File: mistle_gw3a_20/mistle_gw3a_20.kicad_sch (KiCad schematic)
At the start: 55 parts, among them J1 SWD, J2 USB_C_Receptacle_USB2.0, SW1 Boot, U1 SY8113BADC, U2 W25Q64JVS, U3 USBLC6-2SC6, U4 RP2040, Y1 12MHz

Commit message: Update gw3a dev board
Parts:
- removed JP1: SRC D+, Jumper:SolderJumper-3_P1.3mm_Bridged12_RoundedPad1.0x1.5mm, symbol Jumper:SolderJumper_3_Bridged12
- removed JP2: SRC D-, Jumper:SolderJumper-3_P1.3mm_Bridged12_RoundedPad1.0x1.5mm, symbol Jumper:SolderJumper_3_Bridged12
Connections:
- net at U3.1 (I/O1): now also R4.1
- net at U3.3 (I/O2): now also R5.1
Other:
- sheet GW3A-LV20 FPGA ports: added MODE[0..1]; removed none
- note added: "TODO: Use SD-1Bit nomenclature"

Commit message: Update gw3a 20 dev board
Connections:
- net +1V1 renamed +1.1V
- net +3V3 renamed +3.3V
- net SD_DI renamed SD_DAT1
- net SD_DO renamed SD_DAT0
- net ~{SD_CS} renamed SD_DAT3
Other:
- sheet GW3A-LV20 FPGA ports: added SD_CMD, SD_DAT[0..3]; removed SD_DI, SD_DO, ~{SD_CS}
- note added: "SD_DI"
- note added: "SD_DO"
- note added: "~{SD_CS}"

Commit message: Update gw3a dev board
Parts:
- C1, C10, C11, C12, C13, C14, C2, C3, C5, C51, C52, C53, C54, C55, C56, C57, C6, C7, C8, C9, D1, D2, D3, D4, J1, J2, L3, R1, R10, R11, R12, R2, R3, R4, R5, R51, R54, R55, R6, R7, R8, R9, SW1, U1, U3, U4, Y1: checked once -> (none)
- R53: LCSC Part # C11702 -> C25792; checked once -> (none)
- U2: footprint Package_SO:SOIC-8_5.23x5.23mm_P1.27mm -> Package_SO:SOIC-8_5.3x5.3mm_P1.27mm; LCSC Part # (none) -> C179171; checked once -> (none)
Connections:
- net SD_DAT1 is gone; now on net SD_CMD: U4.14 (GPIO11)
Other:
- note removed: "SD_DI"
- note removed: "SD_DO"
- note removed: "~{SD_CS}"

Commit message: Update gw3a board
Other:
- note removed: "TODO: Use SD-1Bit nomenclature"
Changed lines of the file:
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@@
-		)
-	)
-	(text "TODO: Use SD-1Bit nomenclature"
-		(exclude_from_sim no)
-		(at 207.518 91.694 0)
-		(effects
-			(font
-				(size 1.27 1.27)
-			)
 		)
 	)

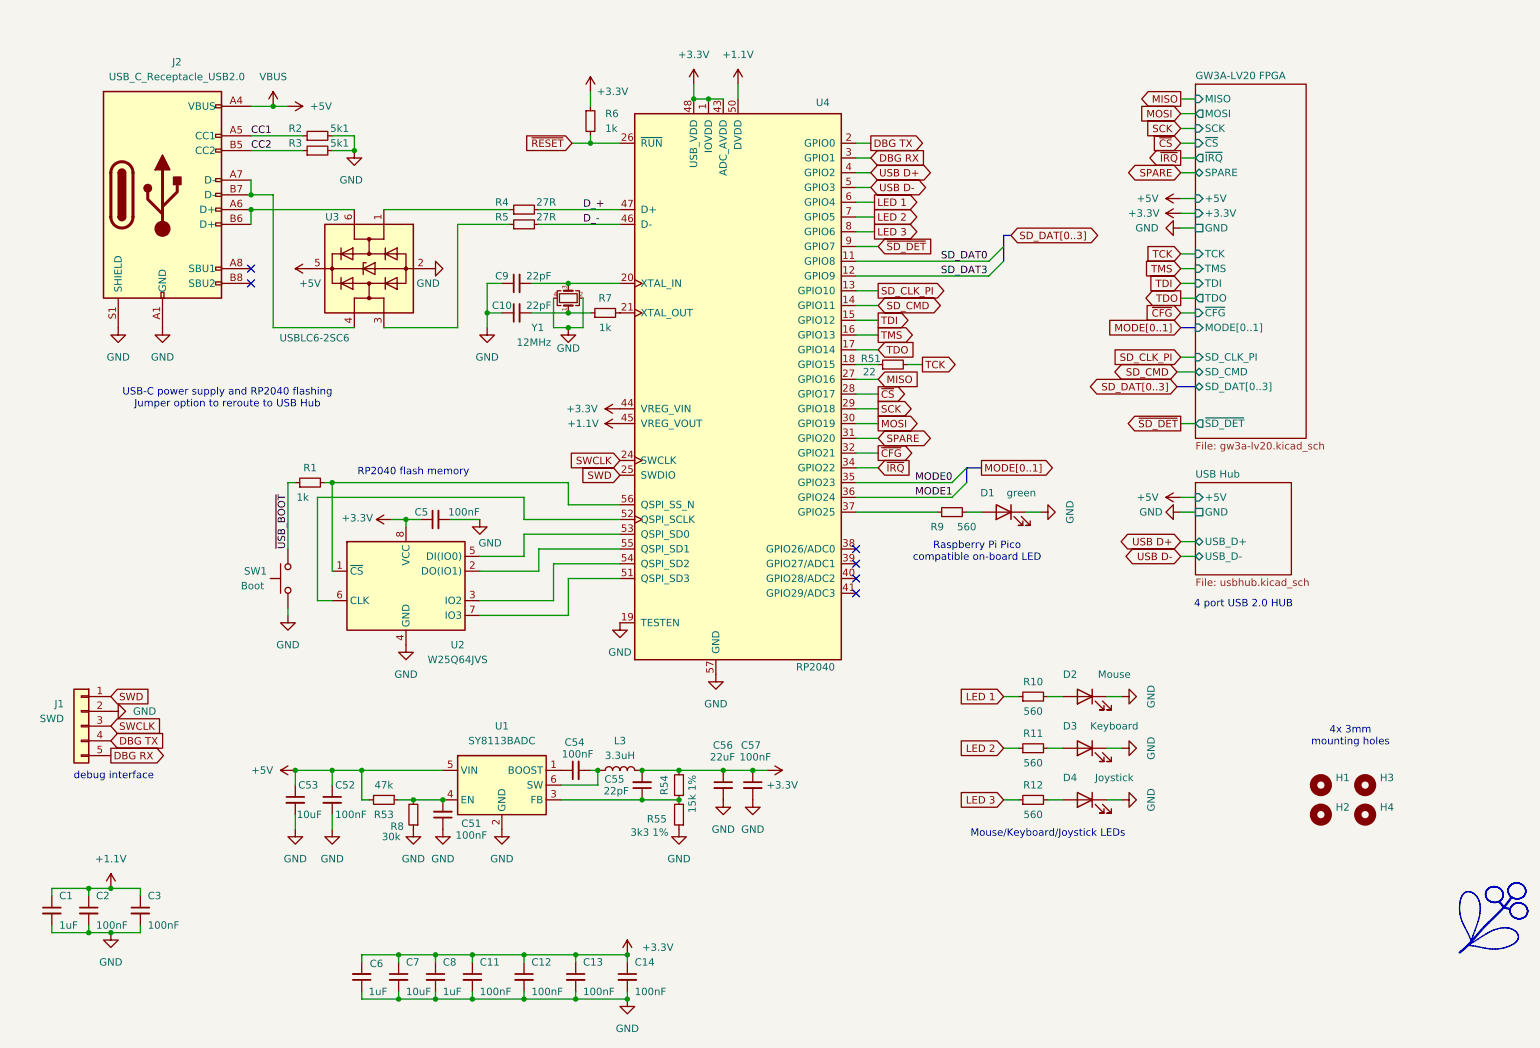
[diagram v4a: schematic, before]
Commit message: Update mistle-gw3a board for rp2350
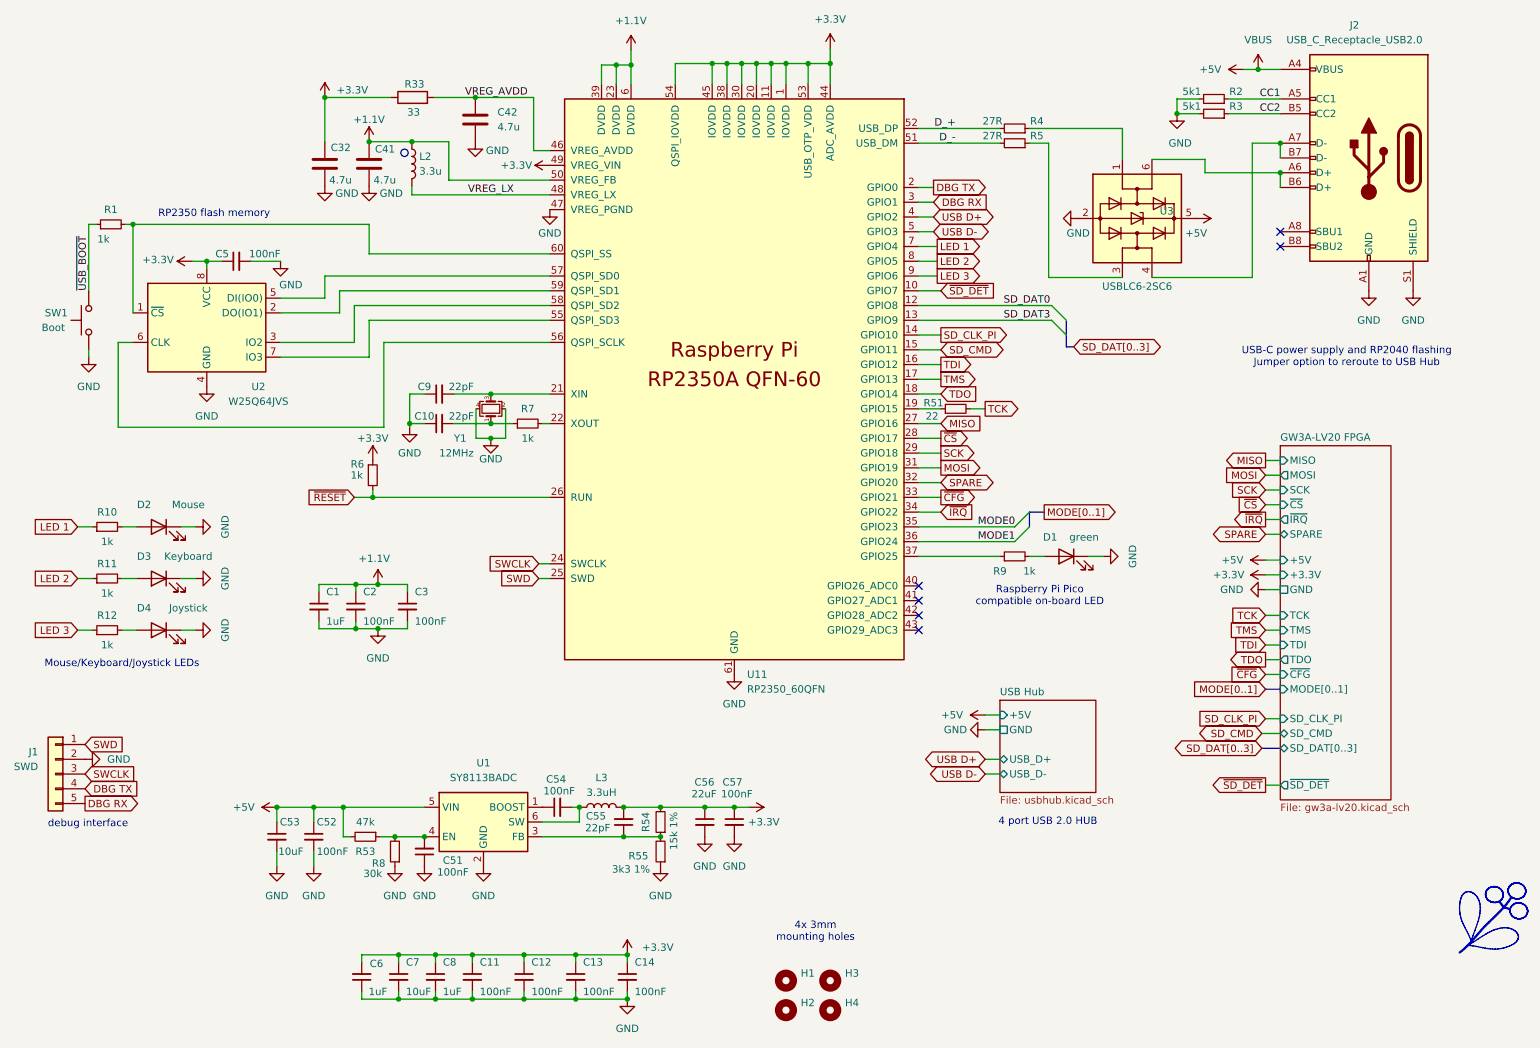
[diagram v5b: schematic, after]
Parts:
- removed U4: RP2040, Sleep-Lib:RP2040-QFN-56, symbol Sleep-lib:RP2040
- added C32, C41, C42: 4.7u, Capacitor_SMD:C_0402_1005Metric, symbol Device:C
- added L2: 3.3u, Inductor_SMD:L_Changjiang_FTC201610D, symbol Device:L
- added R33: 33, Resistor_SMD:R_0402_1005Metric, symbol Device:R
- added U11: RP2350_60QFN, RP2350_60QFN_minimal:RP2350-QFN-60-1EP_7x7_P0.4mm_EP3.4x3.4mm_ThermalVias, symbol MCU_RaspberryPi_RP2350:RP2350_60QFN
- R10, R11, R12, R9: value 560 -> 1k; LCSC Part # C163460 -> C11702
- Y1: LCSC Part # C9002 -> C20625731
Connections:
- net +1.1V: now also C41.1, L2.1, U11.23 (DVDD), U11.39 (DVDD), U11.50 (VREG_FB), U11.6 (DVDD)
- net +3.3V: now also C32.1, R33.1, U11.1 (IOVDD), U11.11 (IOVDD), U11.20 (IOVDD), U11.30 (IOVDD), U11.38 (IOVDD), U11.44 (ADC_AVDD), U11.45 (IOVDD), U11.49 (VREG_VIN), U11.53 (USB_OTP_VDD), U11.54 (QSPI_IOVDD)
- net DBG RX: now also U11.3 (GPIO1)
- net DBG TX: now also U11.2 (GPIO0)
- net D_+: now also U11.52 (USB_DP)
- net D_-: now also U11.51 (USB_DM)
- net GND: now also C32.2, C41.2, C42.2, U11.47 (VREG_PGND), U11.61 (GND)
- net LED 1: now also U11.7 (GPIO4)
- net LED 2: now also U11.8 (GPIO5)
- net LED 3: now also U11.9 (GPIO6)
- net MISO: now also U11.27 (GPIO16)
- net MODE0: now also U11.35 (GPIO23)
- net MODE1: now also U11.36 (GPIO24)
- net MOSI: now also U11.31 (GPIO19)
- net SCK: now also U11.29 (GPIO18)
- net SD_CLK_PI: now also U11.14 (GPIO10)
- net SD_CMD: now also U11.15 (GPIO11)
- net SD_DAT0: now also U11.12 (GPIO8)
- net SD_DAT3: now also U11.13 (GPIO9)
- net SPARE: now also U11.32 (GPIO20)
- net SWCLK: now also U11.24 (SWCLK)
- net SWD: now also U11.25 (SWD)
- net TDI: now also U11.16 (GPIO12)
- net TDO: now also U11.18 (GPIO14)
- net TMS: now also U11.17 (GPIO13)
- net USB D+: now also U11.4 (GPIO2)
- net USB D-: now also U11.5 (GPIO3)
- net ~{CFG}: now also U11.33 (GPIO21)
- net ~{CS}: now also U11.28 (GPIO17)
- net ~{IRQ}: now also U11.34 (GPIO22)
- net ~{RESET}: now also U11.26 (RUN)
- net ~{SD_DET}: now also U11.10 (GPIO7)
- net at R51.1: now also U11.19 (GPIO15)
- net at C9.2, Y1.3: now also U11.21 (XIN)
- net at R7.2: now also U11.22 (XOUT)
- net at R9.1: now also U11.37 (GPIO25)
- net at U2.7 (IO3): now also U11.55 (QSPI_SD3)
- net at U2.6 (CLK): now also U11.56 (QSPI_SCLK)
- net at U2.5 (DI(IO0)): now also U11.57 (QSPI_SD0)
- net at U2.3 (IO2): now also U11.58 (QSPI_SD2)
- net at U2.2 (DO(IO1)): now also U11.59 (QSPI_SD1)
- net at R1.2, U2.1 (~{CS}): now also U11.60 (QSPI_SS)
- new net VREG_AVDD: C42.1, R33.2, U11.46 (VREG_AVDD)
- new net VREG_LX: L2.2, U11.48 (VREG_LX)
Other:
- note added: "RP2350 flash memory"
- note removed: "RP2040 flash memory"
- moved on the sheet: C1, C10, C2, C3, C5, C51, C52, C53, C54, C55, C56, C57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

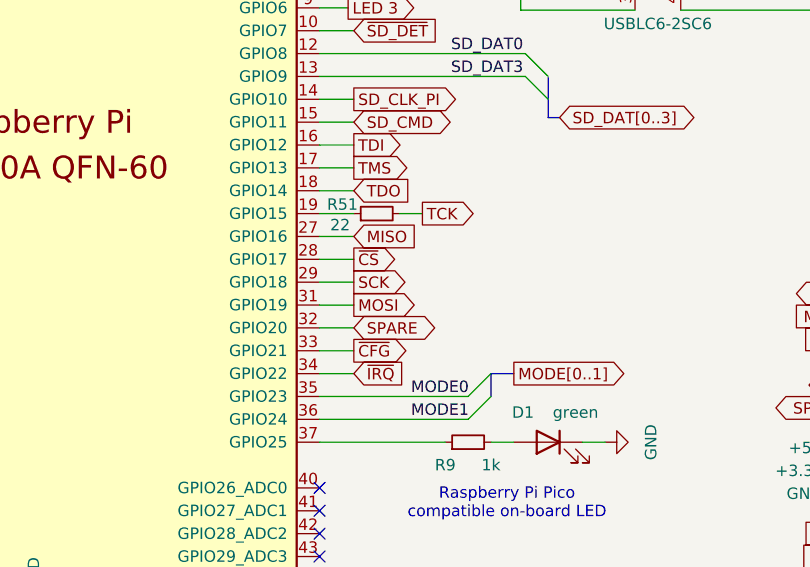
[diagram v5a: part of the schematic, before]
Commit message: Add expansion connector
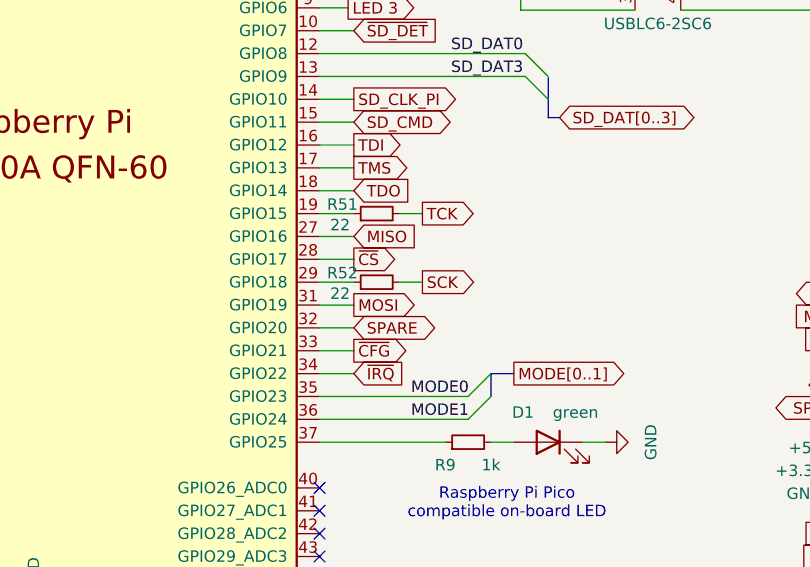
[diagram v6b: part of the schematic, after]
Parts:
- added R52: 22, Resistor_SMD:R_0402_1005Metric, symbol Device:R_Small
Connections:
- net SCK: now also R52.2; no longer U11.29 (GPIO18)
- new net: R52.1, U11.29 (GPIO18)
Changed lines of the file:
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@@
 	(wire
 		(pts
+			(xy 187.325 93.98) (xy 189.865 93.98)
+		)
+		(stroke
+			(width 0)
+			(type default)
+		)
+	)
+	(wire
+		(pts
 			(xy 240.665 35.56) (xy 231.775 35.56)
 		)
@@
 	(global_label "SCK"
 		(shape output)
-		(at 182.245 93.98 0)
+		(at 189.865 93.98 0)
 		(fields_autoplaced yes)
 		(effects
@@
 		)
 		(property "Intersheetrefs" "${INTERSHEET_REFS}"
-			(at 188.9797 93.98 0)
+			(at 196.5997 93.98 0)
 			(hide yes)
 			(show_name no)
@@
 					(unit 1)
 				)
+			)
+		)
+	)
+	(symbol
+		(lib_id "Device:R_Small")
+		(at 184.785 93.98 90)
+		(unit 1)
+		(body_style 1)
+		(exclude_from_sim no)
+		(in_bom yes)
+		(on_board yes)
+		(in_pos_files yes)
+		(dnp no)
+		(property "Reference" "R52"
+			(at 180.975 92.964 90)
+			(show_name no)
+			(do_not_autoplace no)
+			(effects
+				(font
+					(size 1.27 1.27)
+				)
+			)
+		)
+		(property "Value" "22"
+			(at 180.721 95.25 90)
+			(show_name no)
+			(do_not_autoplace no)
+			(effects
+				(font
+					(size 1.27 1.27)
+				)
+			)
+		)
+		(property "Footprint" "Resistor_SMD:R_0402_1005Metric"
+			(at 184.785 93.98 0)
+			(hide yes)
+			(show_name no)
+			(do_not_autoplace no)
+			(effects
+				(font
+					(size 1.27 1.27)
+				)
+			)
+		)
+		(property "Datasheet" ""
+			(at 184.785 93.98 0)
+			(hide yes)
+			(show_name no)
+			(do_not_autoplace no)
+			(effects
+				(font
+					(size 1.27 1.27)
+				)
+			)
+		)
+		(property "Description" ""
+			(at 184.785 93.98 0)
+			(hide yes)
+			(show_name no)
+			(do_not_autoplace no)
+			(effects
+				(font
+					(size 1.27 1.27)
+				)
+			)
+		)
+		(property "LCSC Part #" "C25092"
+			(at 184.785 93.98 90)
+			(hide yes)
+			(show_name no)
+			(do_not_autoplace no)
+			(effects
+				(font
+					(size 1.27 1.27)
+				)
+			)
+		)
+		(pin "1"
+		)
+		(pin "2"
+		)
+		(instances
+			(project "mistle_gw3a_20"
+				(path "/ba62e47e-9e07-4e97-ab08-24b670d50f97"
+					(reference "R52")
+					(unit 1)
+				)

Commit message: Adjust orientation of L2 in the JLC production data. Cudos to JLC for pointing that out
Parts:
- L2: FT Rotation Offset (none) -> 180
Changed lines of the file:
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@@
+			)
+		)
+		(property "FT Rotation Offset" "180"
+			(at 91.186 44.196 0)
+			(hide yes)
+			(show_name no)
+			(do_not_autoplace no)
+			(effects
+				(font
+					(size 1.27 1.27)
+				)
 			)
 		)
